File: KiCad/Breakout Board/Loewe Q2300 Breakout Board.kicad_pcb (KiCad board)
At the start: 2 copper layers, 61 x 12.7 mm, 2 parts, among them J1 VGA DSUB-15, J2 JST_XH_1x10_P2.50mm_Horizontal

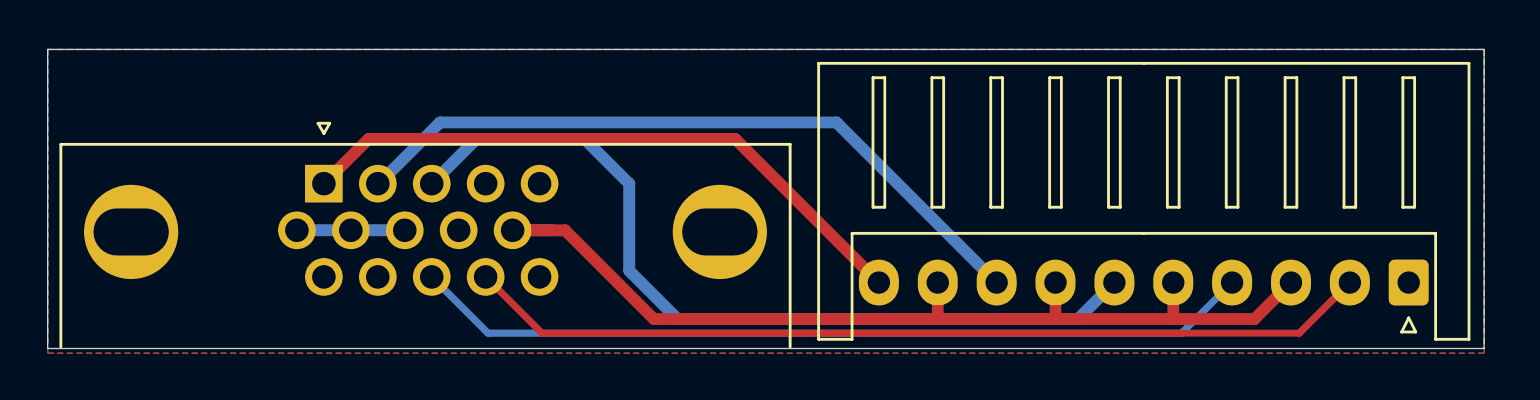
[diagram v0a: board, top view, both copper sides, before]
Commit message: Replace JST XH 2.50 mm with custom 2.54 mm.
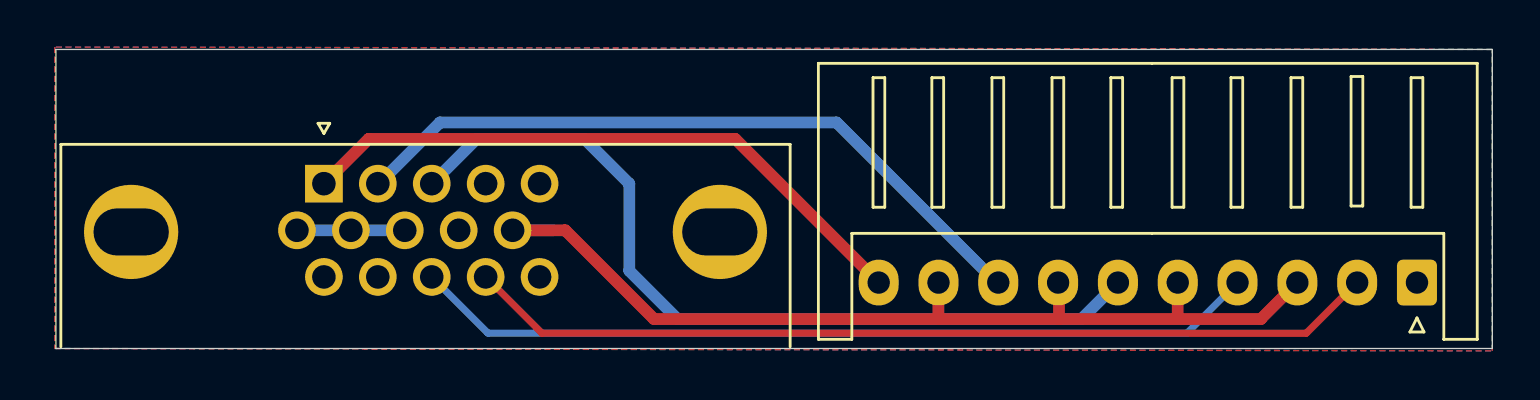
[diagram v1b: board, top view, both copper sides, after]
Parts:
- J2: value JST_XH_1x10_P2.50mm_Horizontal -> JST_XH_1x10_P2.54mm_Horizontal; footprint Connector_JST:JST_XH_S10B-XH-A_1x10_P2.50mm_Horizontal -> JST_XH_S10B_2.54mm:JST_XH_S10B-XH-A_1x10_P2.54mm_Horizontal
- moved J2 0.35 mm to (159.6, 100.7)
